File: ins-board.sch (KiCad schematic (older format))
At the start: 84 parts, among them Q1 FDN306P, U2 STM32F415RGT6, U6 LT1761-3.3, U7 LT1965, X1 CRYSTAL 16MHz 10ppm

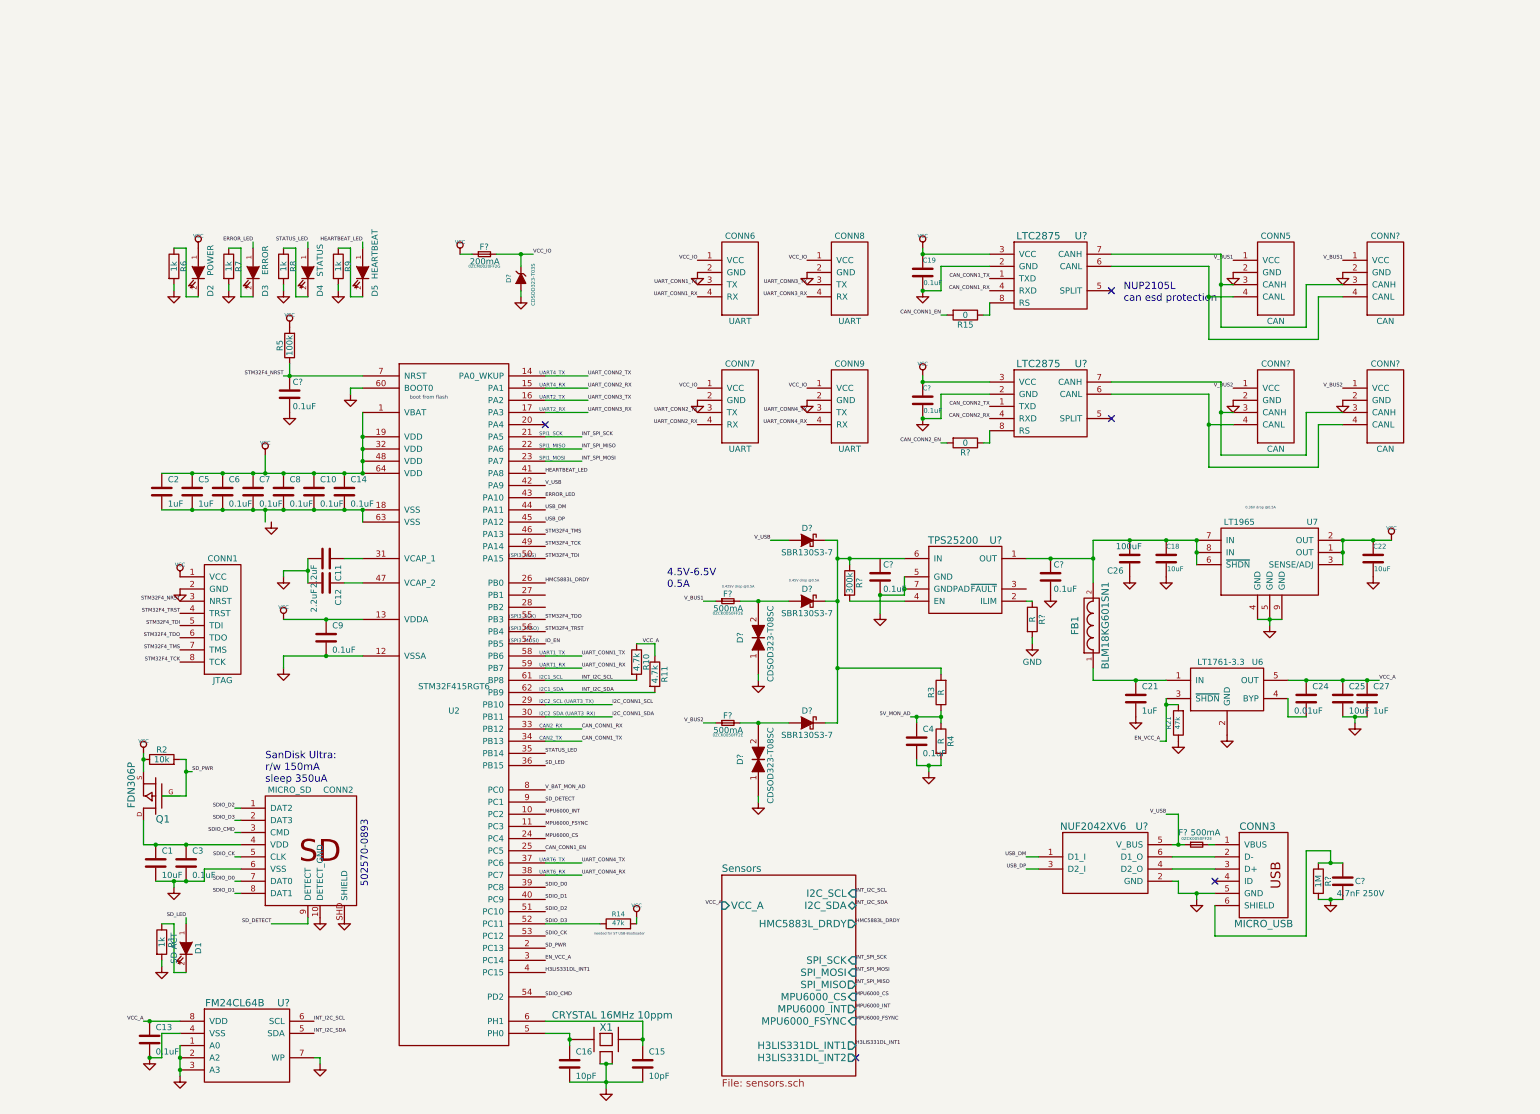
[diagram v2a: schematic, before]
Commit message: CAN pins
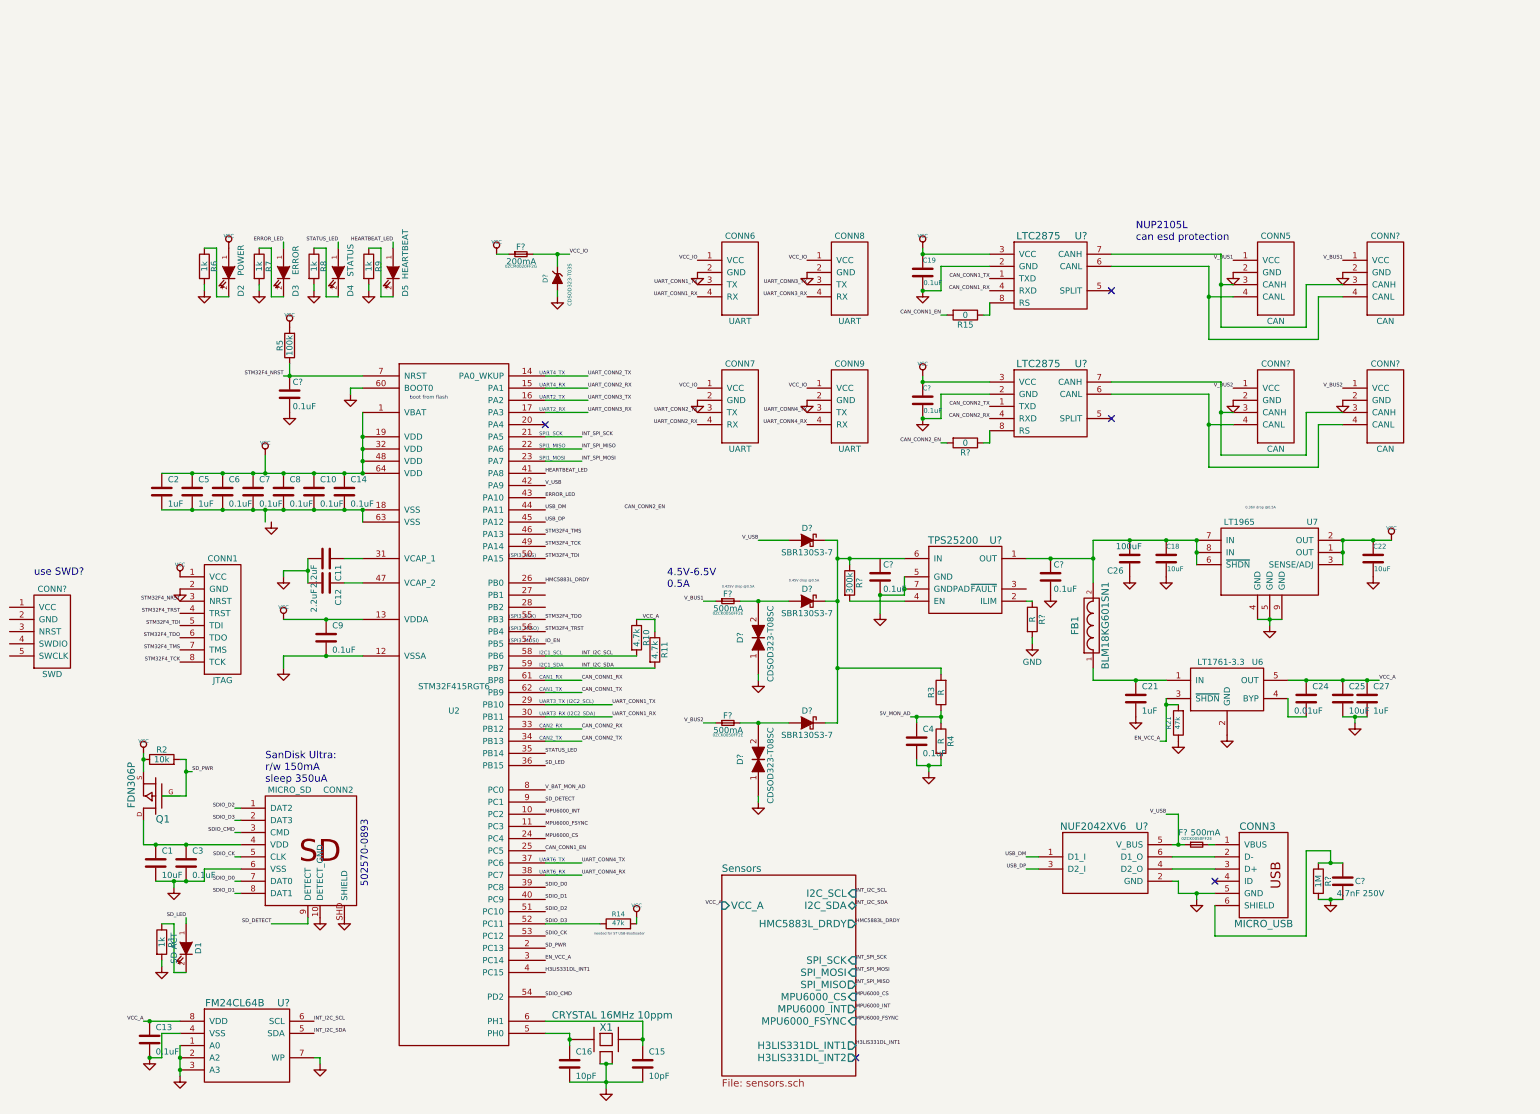
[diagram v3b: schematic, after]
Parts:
- added CONN?: SWD, MODULE, symbol SWD
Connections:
- net I2C_CONN1_SCL is gone; now on net UART_CONN1_TX: U2.29 (PB10)
- net I2C_CONN1_SDA is gone; now on net UART_CONN1_RX: U2.30 (PB11)
- net CAN_CONN1_RX: now also U2.61 (BP8); no longer U2.33 (PB12)
- net CAN_CONN1_TX: now also U2.62 (PB9); no longer U2.34 (PB13)
- net CAN_CONN2_RX: now also U2.33 (PB12)
- net CAN_CONN2_TX: now also U2.34 (PB13)
- net GND: now also CONN?.MECH (GND)
- net INT_I2C_SCL: now also U2.58 (PB6); no longer U2.61 (BP8)
- net INT_I2C_SDA: now also U2.59 (PB7); no longer U2.62 (PB9)
- net UART_CONN1_RX: no longer U2.59 (PB7)
- net UART_CONN1_TX: no longer U2.58 (PB6)
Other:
- note added: "CAN1_RX"
- note added: "CAN1_TX"
- note added: "UART3_RX (I2C2_SDA)"
- note added: "UART3_TX (I2C2_SCL)"
- note added: "use SWD?"
- note removed: "I2C2_SCL (UART3_TX)"
- note removed: "I2C2_SDA (UART3_RX)"
- note removed: "UART1_RX"
- note removed: "UART1_TX"
- moved on the sheet: D2, D3, D4, D5, D?, F?, R10, R11, R6, R7, R8, R9

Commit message: STM32 pins
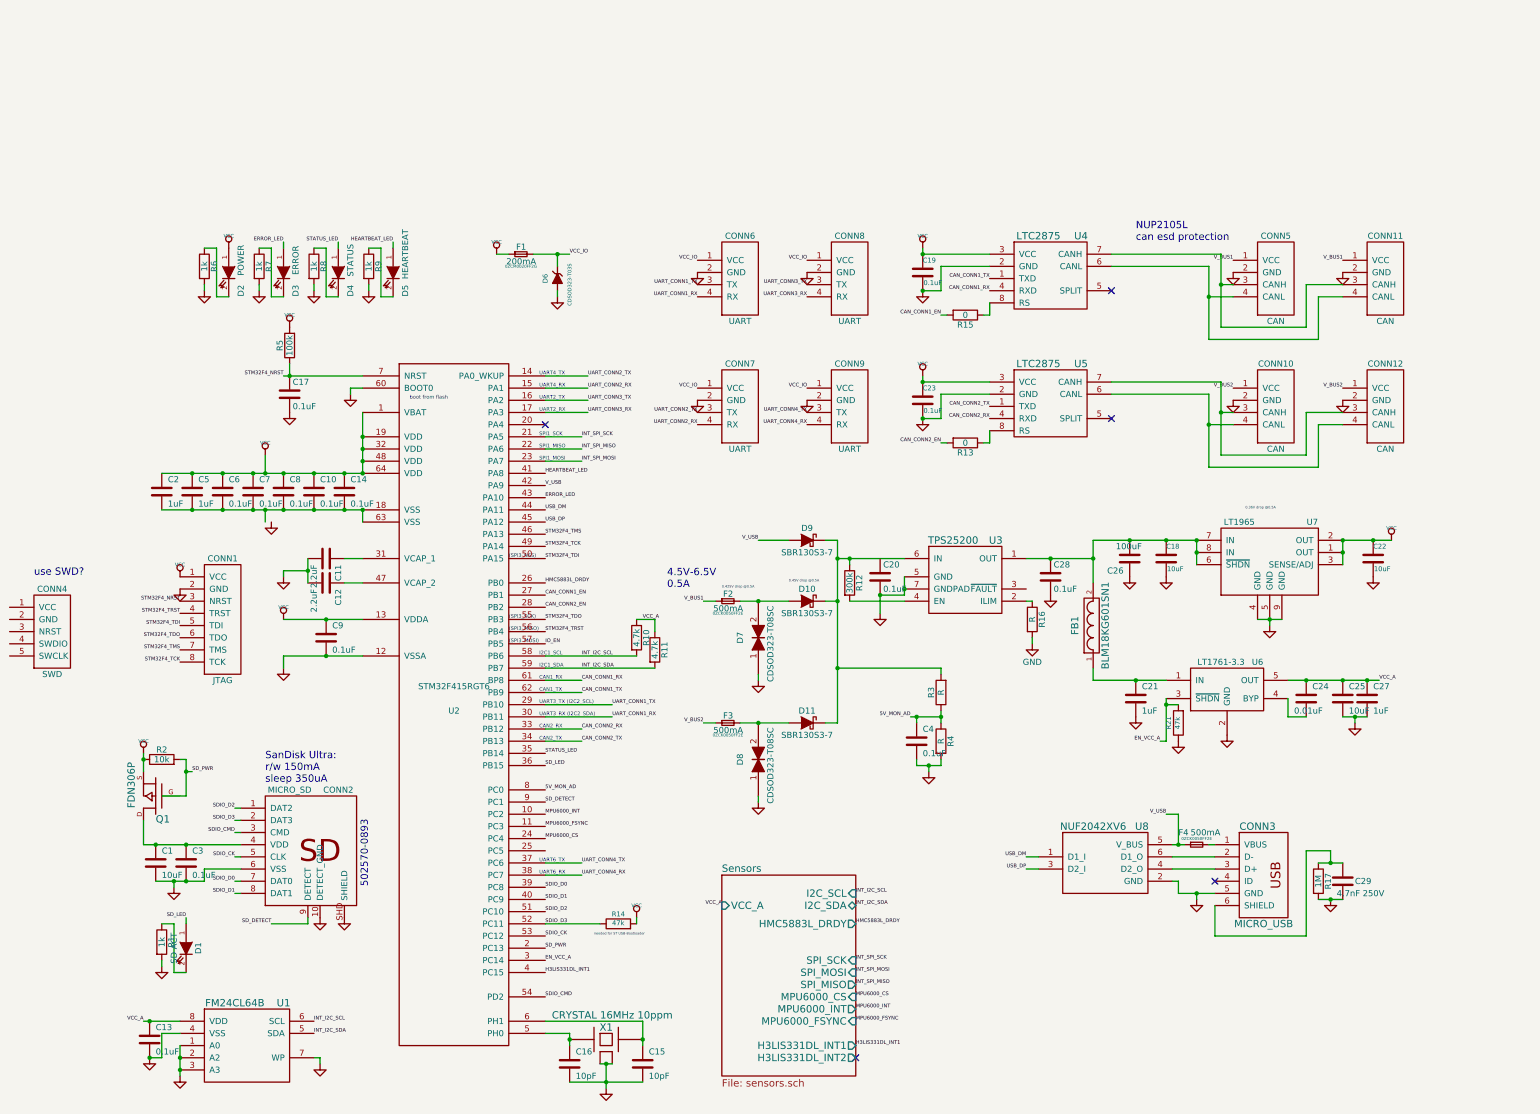
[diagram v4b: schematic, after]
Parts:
- gave numbers to parts that had none: 28
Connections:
- net V_BAT_MON_AD is gone; now on net 5V_MON_AD: U2.8 (PC0)
- net CAN_CONN1_EN: now also U2.27 (PB1); no longer U2.25 (PC5)
- net CAN_CONN2_EN: now also U2.28 (PB2)

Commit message: schematic
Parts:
- added R? (x8): 150, symbol R
- C1, C10, C11, C12, C13, C14, C15, C16, C17, C2, C20, C21, C24, C25, C27, C28, C29, C3, C4, C5, C6, C7, C8, C9, D1, D2, D3, D4, D5, F1, FB1, R1, R10, R11, R12, R13, R15, R16, R17, R2, R3, R4, R5, R6, R7, R8, R9: footprint (none) -> _std:_0603-W
- C18, C19, C22, C23, R14: footprint ~ -> _std:_0603-W
- CONN1: footprint MODULE -> _connectors:_Molex-PicoBlade-SMD-8
- CONN10, CONN11, CONN12: footprint MODULE -> (none)
- CONN2: footprint MODULE -> _div:_Molex-microSD-502570-0893
- CONN3: footprint (none) -> _connectors:_Micro-USB-AB-receptacle-SMT
- CONN4, CONN5, CONN6, CONN7, CONN8, CONN9: footprint MODULE -> _connectors:_Molex-PicoBlade-SMD-4
- D6: footprint (none) -> _std:_SC79
- Q1: footprint (none) -> _div:_FAIRCHILD-MOSFET-SuperSOT-3
- U1: footprint (none) -> _std:_TSSOP-8
- U2: footprint MODULE -> _lqfp:_LQFP64
- U3: footprint (none) -> _std:_TSOT23-6
- U4: footprint (none) -> _std:_SOT23-8
- U5: footprint (none) -> _std:_MSOP-8-EP
- U6: footprint MODULE -> _std:_TSOT23-5
- U7: footprint MODULE -> _std:_MSOP-8-EP
- U8: footprint (none) -> _sensors:_MS5611-01BA
- X1: footprint (none) -> _div:_TSX-3225-SMD-XTAL
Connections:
- net UART_CONN1_RX: now also R?.1; no longer CONN6.4 (RX)
- net UART_CONN1_TX: now also R?.1; no longer CONN6.3 (TX)
- net UART_CONN2_RX: now also R?.1; no longer CONN7.4 (RX)
- net UART_CONN2_TX: now also R?.1; no longer CONN7.3 (TX)
- net UART_CONN3_RX: now also R?.1; no longer CONN8.4 (RX)
- net UART_CONN3_TX: now also R?.1; no longer CONN8.3 (TX)
- net UART_CONN4_RX: now also R?.1; no longer CONN9.4 (RX)
- net UART_CONN4_TX: now also R?.1; no longer CONN9.3 (TX)
- new net: CONN6.3 (TX), R?.2
- new net: CONN6.4 (RX), R?.2
- new net: CONN7.3 (TX), R?.2
- new net: CONN7.4 (RX), R?.2
- new net: CONN8.3 (TX), R?.2
- new net: CONN8.4 (RX), R?.2
- new net: CONN9.3 (TX), R?.2
- new net: CONN9.4 (RX), R?.2
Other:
- note added: "ESD protection\n& EMI filter"
- moved on the sheet: C19, C23, CONN6, CONN7, CONN8, CONN9, R13, R15, U4, U5

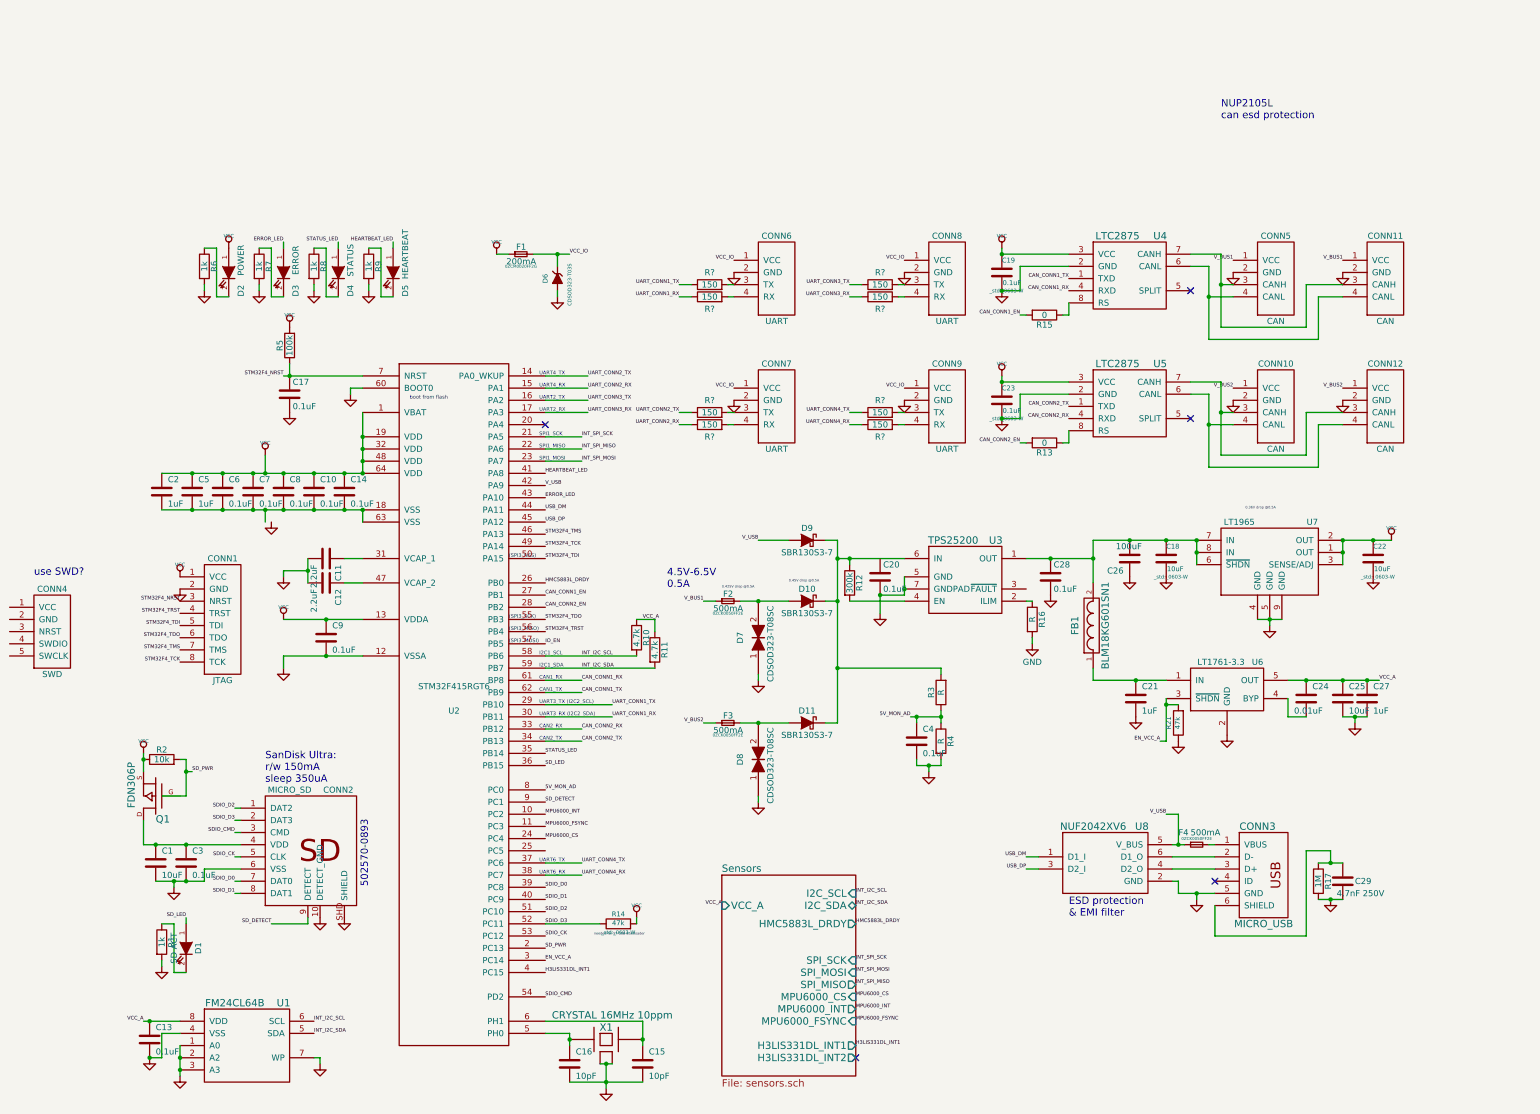
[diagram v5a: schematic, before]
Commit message: comments power supply changes
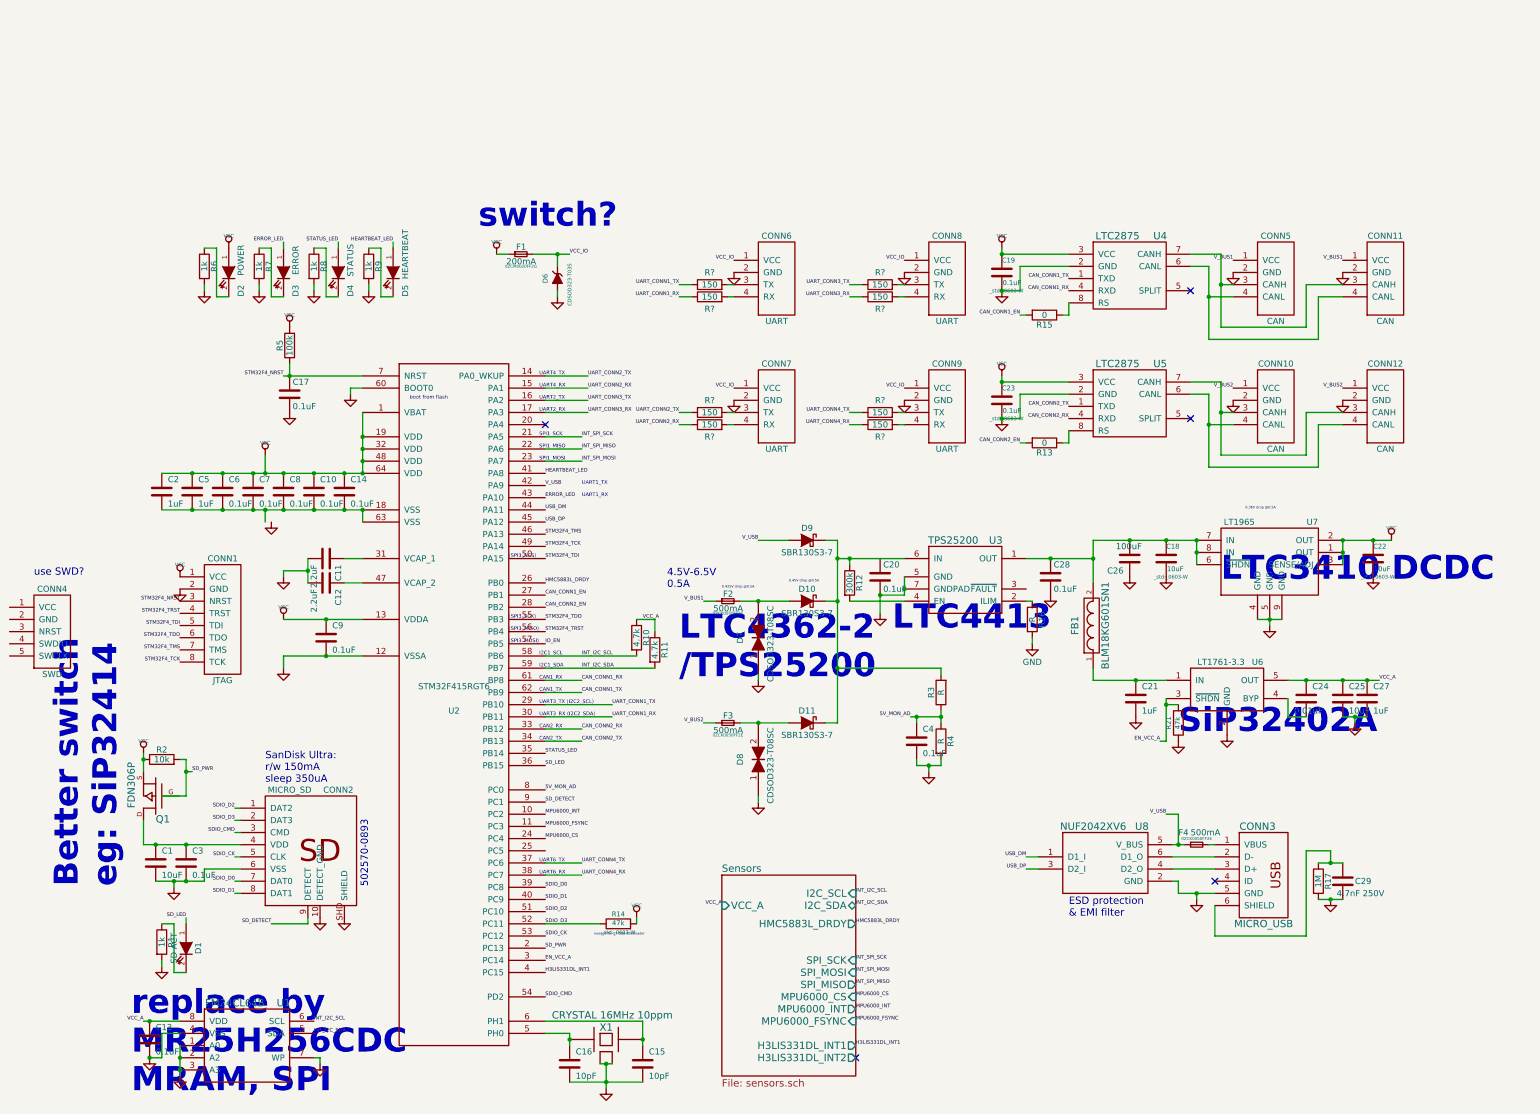
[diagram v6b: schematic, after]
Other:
- note added: "Better switch\neg: SiP32414 \n"
- note added: "LTC3410 DCDC"
- note added: "LTC4362-2\n/TPS25200"
- note added: "LTC4413"
- note added: "SiP32402A"
- note added: "UART1_RX"
- note added: "UART1_TX"
- note added: "replace by\nMR25H256CDC\nMRAM, SPI"
- note added: "switch?"
- note removed: "NUP2105L \ncan esd protection"
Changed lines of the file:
@@
 LIBS:memory
 LIBS:xilinx
-LIBS:special
 LIBS:microcontrollers
 LIBS:dsp
@@
 Wire Wire Line
 	3850 800  4150 800
-Text Notes 9500 -300 0    60   ~ 0
-NUP2105L \ncan esd protection
 $Comp
 L GND #PWR22
@@
 Wire Wire Line
 	9250 1950 9400 1950
+Text Notes 9150 4750 0    197  ~ 39
+SiP32402A
+Text Notes 450  6000 1    197  ~ 39
+Better switch\neg: SiP32414 \n
+Text Notes 6800 3900 0    197  ~ 39
+LTC4413
+Text Notes 5050 4300 0    197  ~ 39
+LTC4362-2\n/TPS25200
+Text Notes 3400 600  0    197  ~ 39
+switch?
+Text Notes 550  7700 0    197  ~ 39
+replace by\nMR25H256CDC\nMRAM, SPI
+Text Notes 9500 3500 0    197  ~ 39
+LTC3410 DCDC
+Text Notes 4250 2700 0    30   ~ 0
+UART1_TX
+Text Notes 4250 2800 0    30   ~ 0
+UART1_RX
 $EndSCHEMATC
